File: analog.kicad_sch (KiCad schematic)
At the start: 36 parts, among them IC6 MCP6S91-E_MS, IC7 MCP6S91-E_MS, IC8 MCP4726A0T-E_CH, K1 AQY210EHAX, K2 AQY210EHAX, U10 MCP6022T-I_SN, U8 MCP6022T-I_SN, U9 MCP6022T-I_SN

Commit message: last changes
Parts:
- removed D10, D7, D8, D9: D_Schottky, Diode_SMD:D_0805_2012Metric_Pad1.15x1.40mm_HandSolder, symbol Device:D_Schottky
- added D7: BAT54S, Package_TO_SOT_SMD:SOT-23, symbol Diode:BAT54S
- added D8: (no value), symbol Diode:BAT54S
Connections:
- net +3.3VA: now also D7.2, D8.2
- net GNDA: now also D7.1, D8.1
- net at C27.1, C29.1, R23.1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: now also D8.3
- net at C26.1, C28.1, R22.1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: now also D7.3

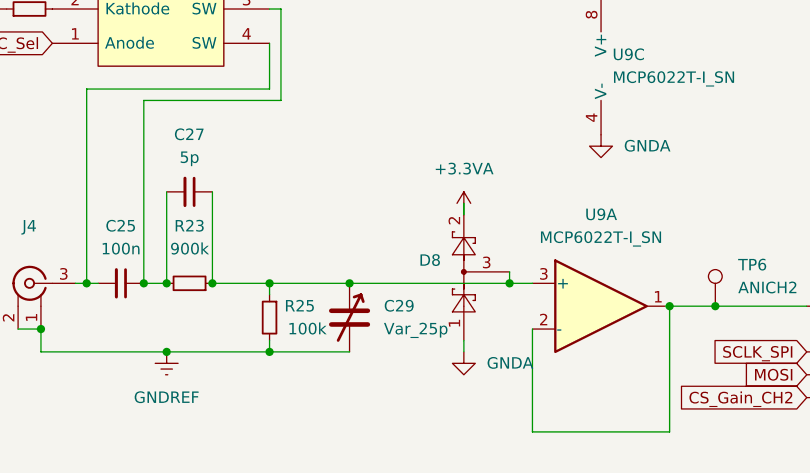
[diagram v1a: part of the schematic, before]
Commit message: fixed uart connection
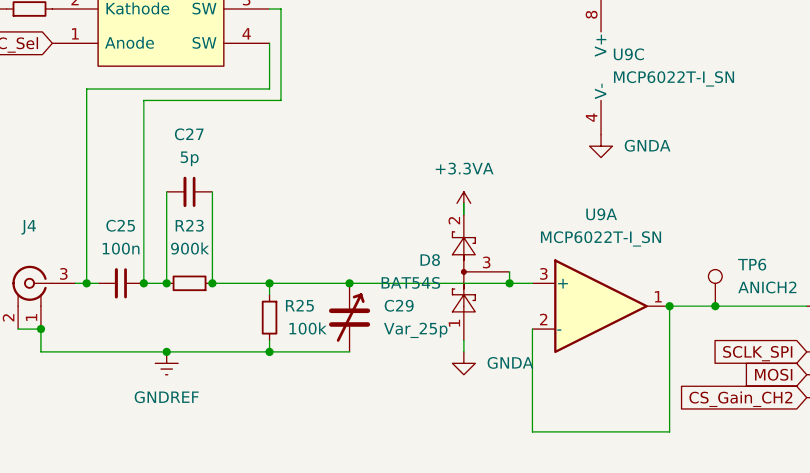
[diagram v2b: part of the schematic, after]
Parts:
- D8: value (none) -> BAT54S; footprint (none) -> Package_TO_SOT_SMD:SOT-23
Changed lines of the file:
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@@
       (effects (font (size 1.27 1.27)) (justify left))
     )
-    (property "Value" "" (id 1) (at 74.93 142.2399 90)
+    (property "Value" "BAT54S" (id 1) (at 74.93 142.2399 90)
       (effects (font (size 1.27 1.27)) (justify left))
     )
-    (property "Footprint" "" (id 2) (at 74.295 139.065 0)
+    (property "Footprint" "Package_TO_SOT_SMD:SOT-23" (id 2) (at 74.295 139.065 0)
       (effects (font (size 1.27 1.27)) (justify left) hide)
     )

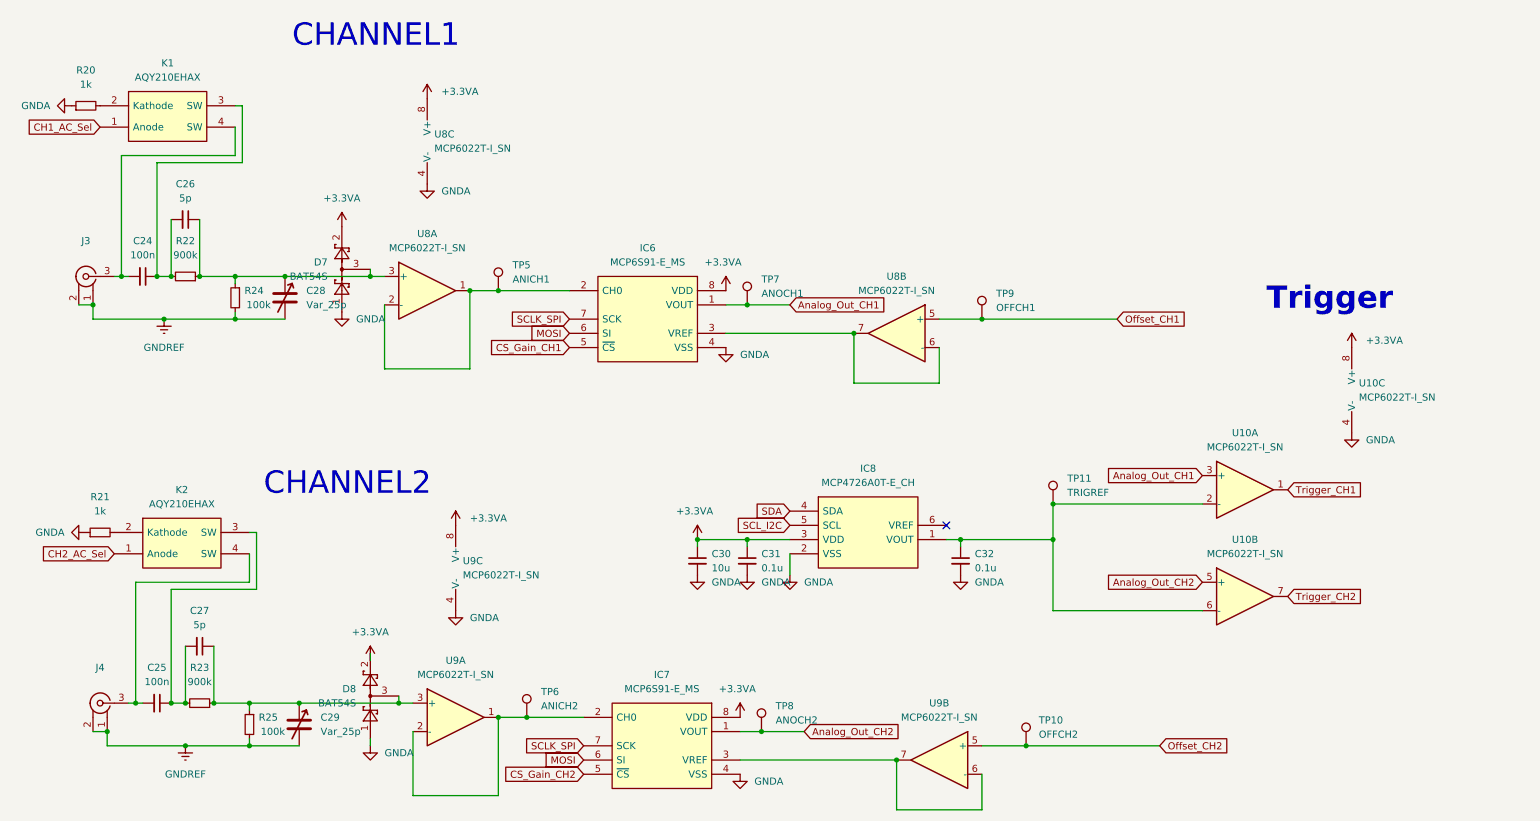
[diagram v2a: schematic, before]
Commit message: changed linear regulators
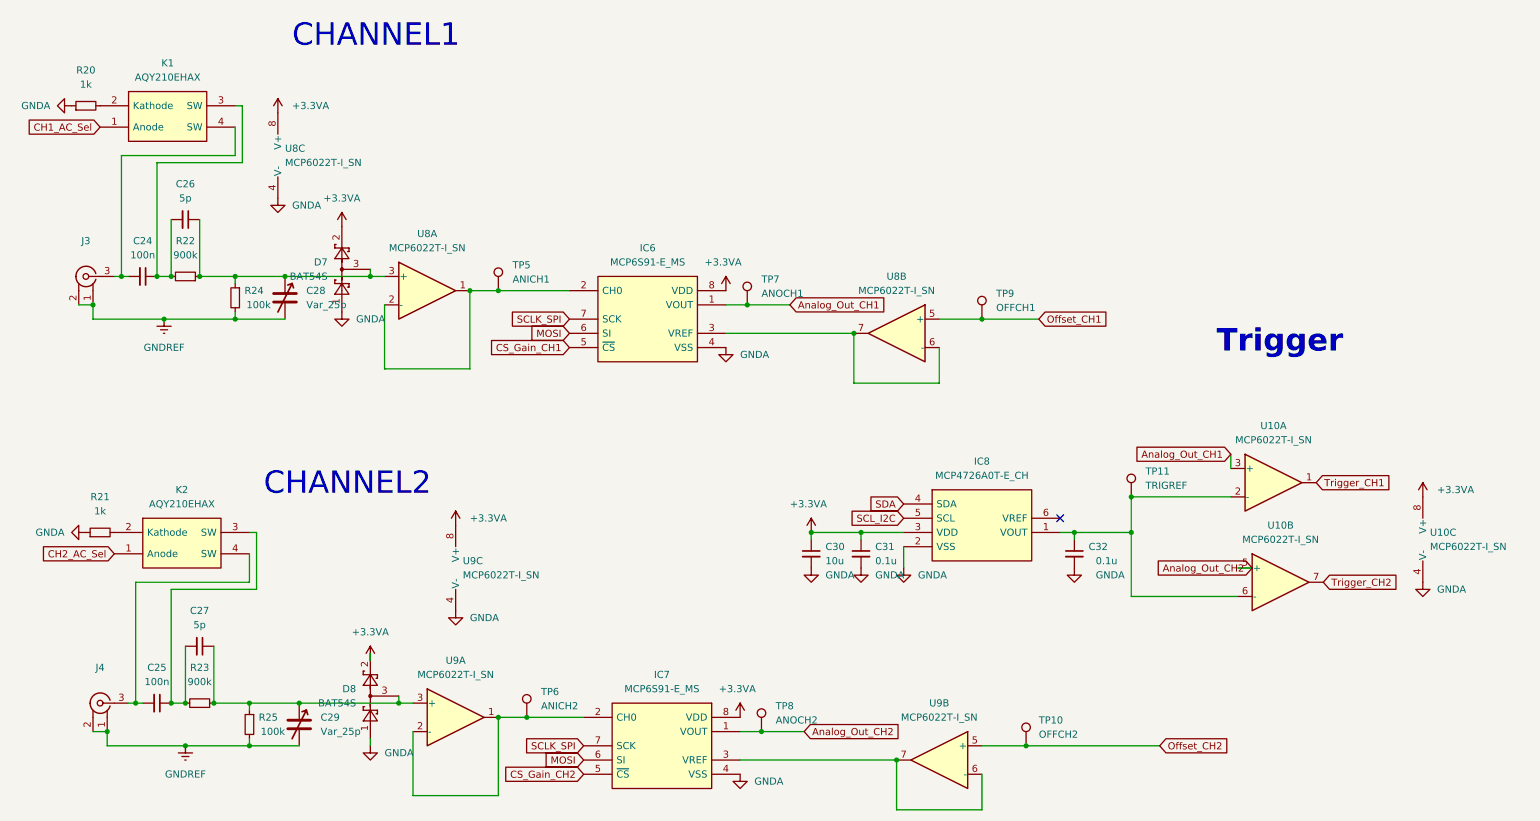
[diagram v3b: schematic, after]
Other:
- moved on the sheet: C30, C31, C32, IC8, TP11, U10A, U10B, U10C, U8C
